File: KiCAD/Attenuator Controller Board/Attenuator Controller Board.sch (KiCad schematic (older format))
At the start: 21 parts, among them J1 Barrel_Jack_Switch, J10 Conn_01x24_Female, J2 Conn_01x02_Female, J9 Conn_01x24_Female, U12 Teensy3.6

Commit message: Rebuild schematic- git can be frustrating sometimes
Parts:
- removed H10: MountingHole_Pad, Custom Footprints:Ref_only, symbol Mechanical:MountingHole_Pad
- removed H9: MountingHole_Pad, Custom Footprints:M2_standoff_ground_via, symbol Mechanical:MountingHole_Pad
- removed J1: Barrel_Jack_Switch, Custom Footprints:DC-jack_54-00165, symbol Connector:Barrel_Jack_Switch
- removed J2: Conn_01x02_Female, Custom Footprints:Wire_Pad, symbol Connector:Conn_01x02_Female
- added C1, C2: 10µF, Custom Footprints:0508_Capacitor, symbol Device:C_Small
- added J5: DSub9, Custom Footprints:K202XHT-E9P-N, symbol Attenuator-Controller-Board-rescue:K202XHT-E9P-N-Custom_parts
- added R1: R_Small, Resistor_SMD:R_0603_1608Metric, symbol Device:R_Small
- J1: renamed from J9; symbol Custom_parts:Conn_01x24_Female -> Attenuator-Controller-Board-rescue:Conn_01x24_Female-Custom_parts
- J2: renamed from J?; value DSub_15_HD_-_200-015-263R001 -> DSub_15_HD; footprint Custom:DSub_15_HD-200-015-263R001 -> Custom Footprints:200-015-263R001; symbol Custom_parts:DSub_15_HD_-_200-015-263R001 -> Attenuator-Controller-Board-rescue:DSub_15_HD_-_200-015-263R001-Custom_parts
- J3, J4: renamed from J?; value K202XHT-E9P-N -> DSub9; footprint Custom:K202XHT-E9P-N -> Custom Footprints:K202XHT-E9P-N; symbol Custom_parts:K202XHT-E9P-N -> Attenuator-Controller-Board-rescue:K202XHT-E9P-N-Custom_parts
- J6: renamed from J10; symbol Custom_parts:Conn_01x24_Female -> Attenuator-Controller-Board-rescue:Conn_01x24_Female-Custom_parts
- U1: renamed from U?; footprint SOIC_7T8TA_DIO -> Custom Footprints:ZXMHC3A01T8TA; symbol Custom_parts:ZXMHC3A01T8TA -> Attenuator-Controller-Board-rescue:ZXMHC3A01T8TA-Custom_parts; Manufacturer (none) -> Diodes Incorporated; Part # (none) -> ZXMHC3A01T8TA
- U2: renamed from U?; footprint Custom:ADM3307EARUZ -> Custom Footprints:ADM3307EARUZ; symbol Custom_parts:ADM3307EARU-REEL7 -> Attenuator-Controller-Board-rescue:ADM3307EARU-REEL7-Custom_parts
- U3: renamed from U12; symbol Custom_parts:Teensy3.6 -> Attenuator-Controller-Board-rescue:Teensy3.6-Custom_parts
- gave numbers to parts that had none: 6
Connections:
- net labels added: Enable, Motor1, Motor2, RS-232_RXD3, RS-232_TXD3, Serial3-RX, Serial3-TX, Shutdown
- net labels removed: Ident(+)
- wire segments 75 -> 74
- no-connect marks 61 -> 63

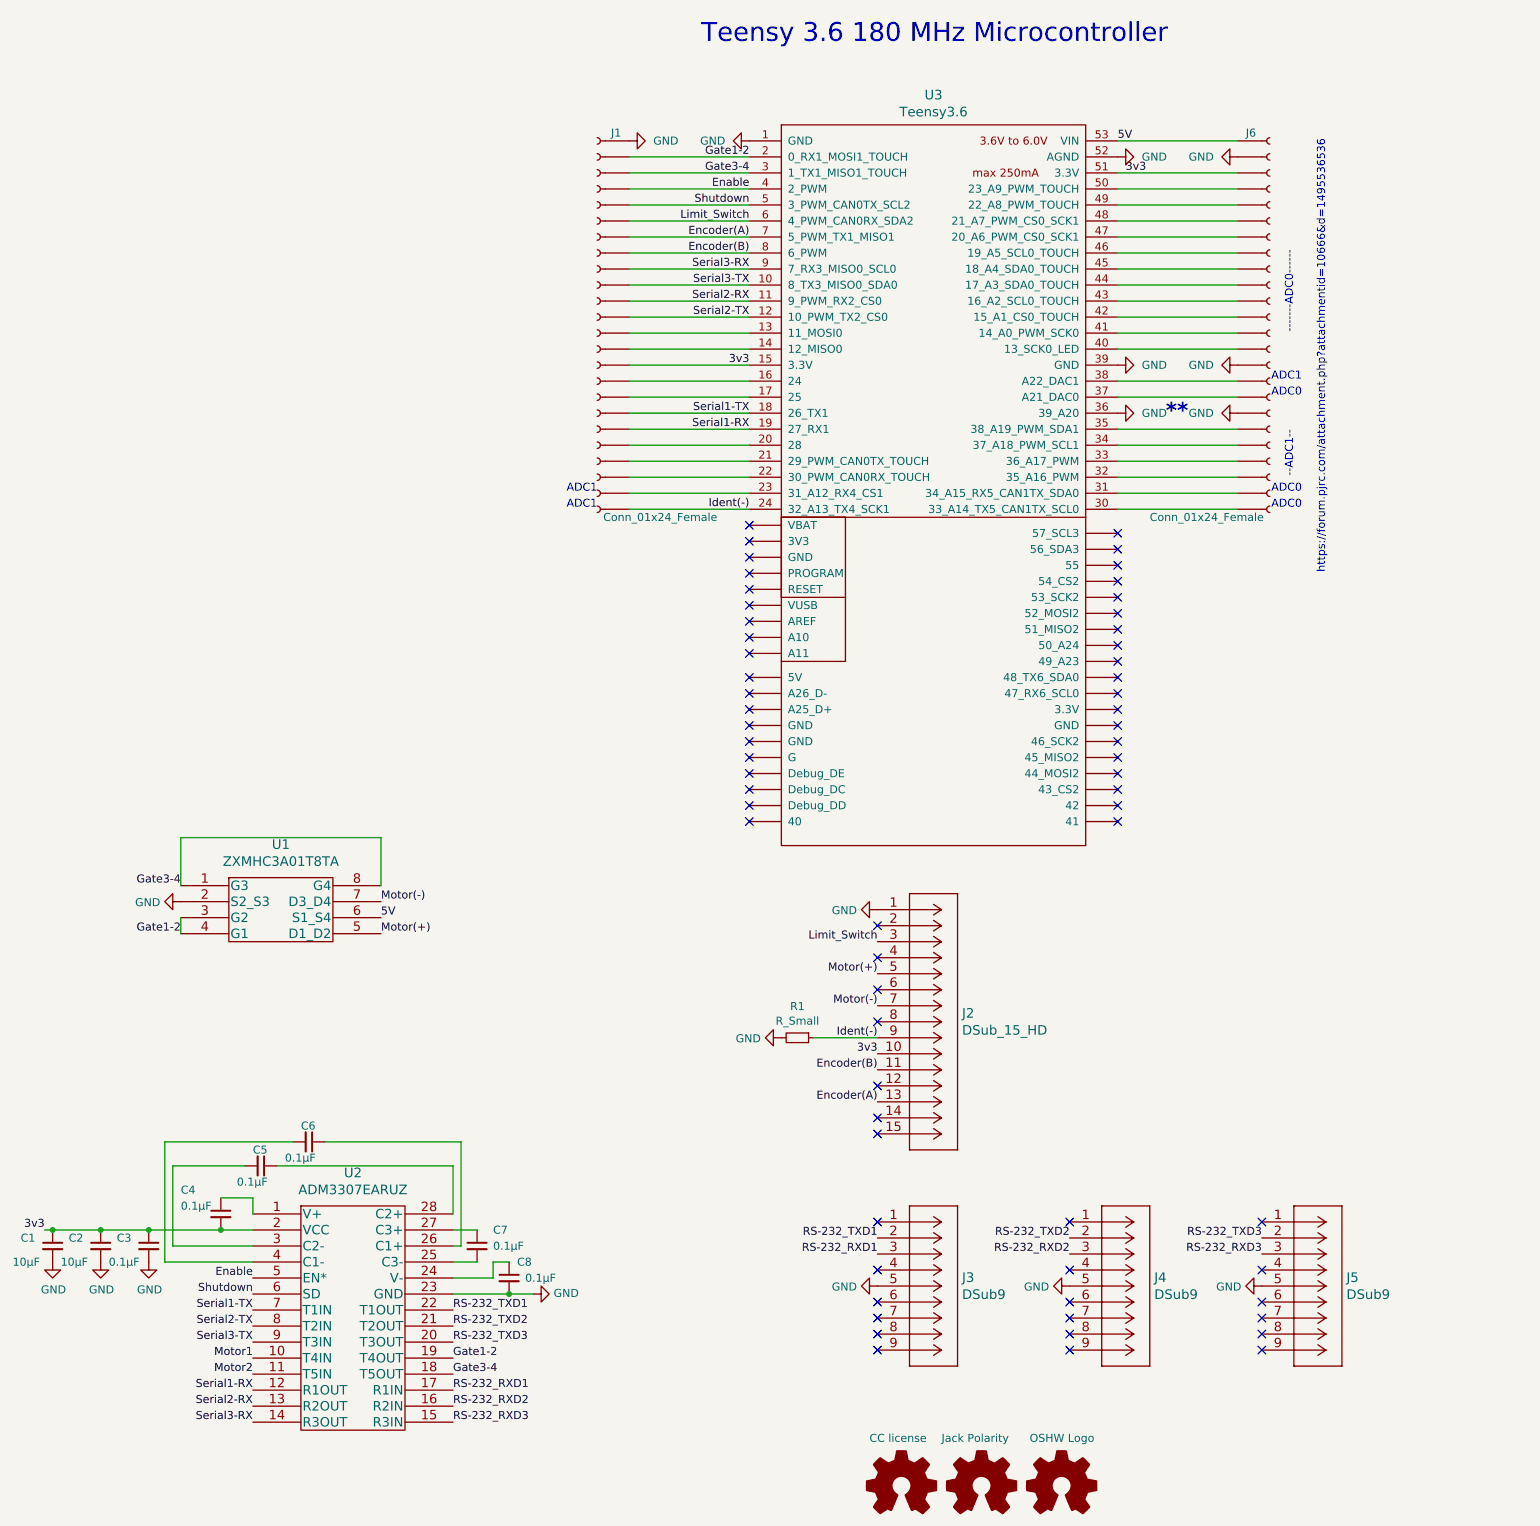
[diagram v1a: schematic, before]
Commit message: BNC clamps and alarm added
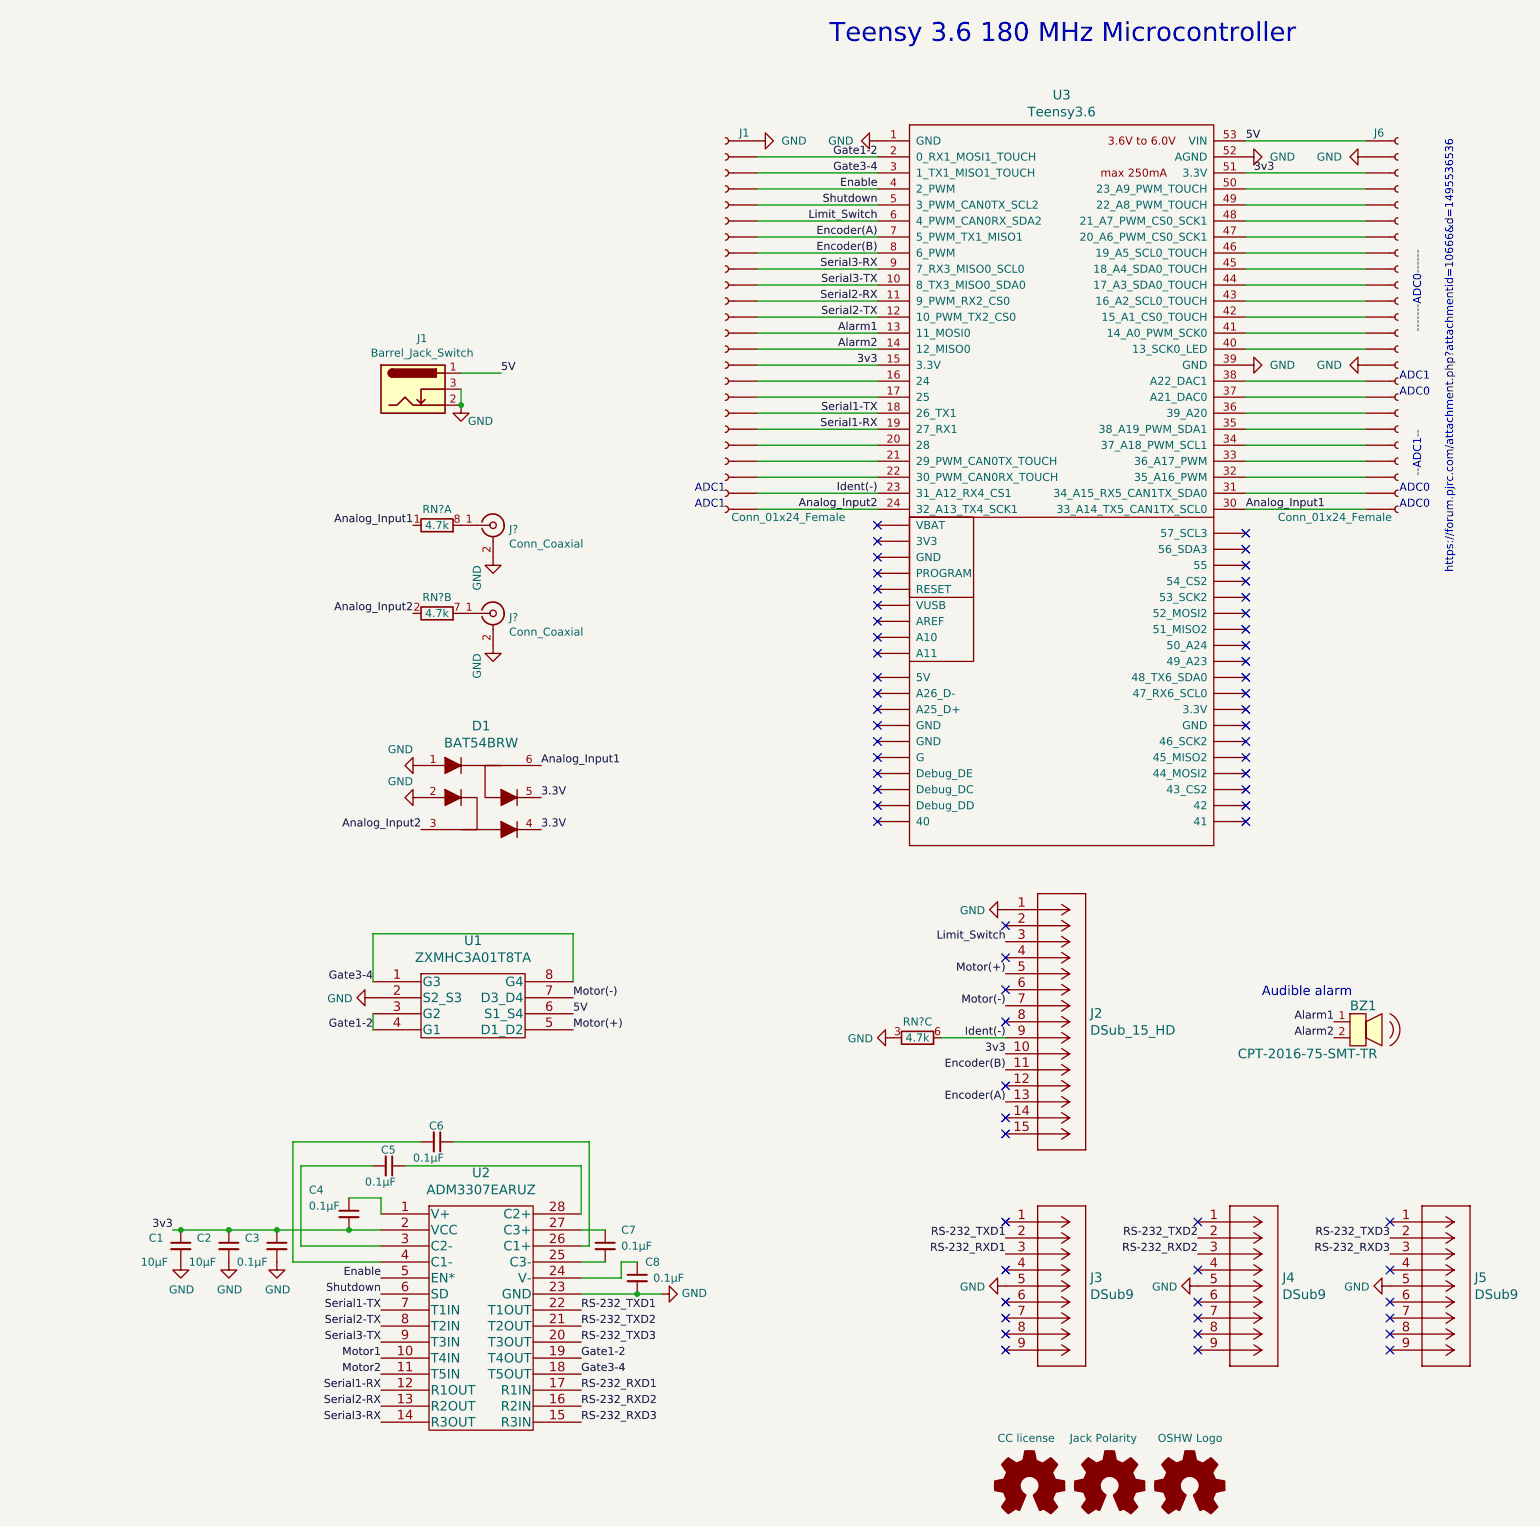
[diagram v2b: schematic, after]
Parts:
- removed R1: R_Small, Resistor_SMD:R_0603_1608Metric, symbol Device:R_Small
- added BZ1: CPT-2016-75-SMT-TR, Custom Footprints:SMT-0940-T-3V-R_9x9_alarm, symbol Custom_parts:CPT-2016-75-SMT-TR
- added D1: BAT54BRW, Package_TO_SOT_SMD:SOT-363_SC-70-6, symbol Custom_parts:BAT54BRW
- added J1: Barrel_Jack_Switch, Custom Footprints:DC-jack_54-00165, symbol Connector:Barrel_Jack_Switch
- added J? (x2): Conn_Coaxial, Custom Footprints:112640, symbol Connector:Conn_Coaxial
- added RN? (x3): 4.7k, Resistor_SMD:R_Array_Convex_4x1206, symbol Device:R_Pack04_Split
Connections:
- net 5V: now also J1.1
- net GND: now also D1.1, D1.2, J1.2, J1.3, J?.2 (Ext), J?.2 (Ext), RN?.3 (R3.1); no longer U3.36 (39_A20)
- net Ident(-): now also U3.23 (31_A12_RX4_CS1), RN?.6 (R3.2); no longer U3.24 (32_A13_TX4_SCK1)
- net Alarm1: now reaches J1.~, U3.13 (11_MOSI0)
- net Alarm1: now also BZ1.1
- net Alarm2: now reaches J1.~, U3.14 (12_MISO0)
- net Alarm2: now also BZ1.2
- net Analog_Input1: now reaches J6.~, U3.30 (33_A14_TX5_CAN1TX_SCL0)
- net Analog_Input1: now also D1.6, RN?.1 (R1.1)
- new net: J?.1 (In), RN?.8 (R1.2)
- new net: J6.~, U3.36 (39_A20)
- new net: J?.1 (In), RN?.7 (R2.2)
- new net 3.3V: D1.4, D1.5
- new net Analog_Input2: D1.3, J1.~, RN?.2 (R2.1), U3.24 (32_A13_TX4_SCK1)
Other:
- note added: "Audible alarm"
- note removed: "**"
- moved on the sheet: C1, C2, C3, C4, C5, C6, C7, C8, J2, J3, J4, J5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

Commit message: Initial PCB layout
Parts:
- added H1, H2, H3, H4: MountingHole, Custom Footprints:1_4-20_Clearance_hole, symbol Mechanical:MountingHole
- gave numbers to parts that had none: 3
- renumbered J1 to J4, J2 to J5, J3 to J6, J4 to J7, J5 to J8, J6 to J9, U2 to U1, U1 to U2
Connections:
- net NC24: now reaches J4.~, U3.16 (24)
- net NC25: now reaches J4.~, U3.17 (25)
- net NC28: now reaches J4.~, U3.20 (28)
- net NC29: now reaches J4.~, U3.21 (29_PWM_CAN0TX_TOUCH)
- net NC30: now reaches J4.~, U3.22 (30_PWM_CAN0RX_TOUCH)
- net NC34: now reaches J9.~, U3.31 (34_A15_RX5_CAN1TX_SDA0)
- net NC35: now reaches J9.~, U3.32 (35_A16_PWM)
- net NC36: now reaches J9.~, U3.33 (36_A17_PWM)
- net NC37: now reaches J9.~, U3.34 (37_A18_PWM_SCL1)
- net NC38: now reaches J9.~, U3.35 (38_A19_PWM_SDA1)
- net NC39: now reaches J9.~, U3.36 (39_A20)
- net NC_DAC0: now reaches J9.~, U3.37 (A21_DAC0)
- net NC_DAC1: now reaches J9.~, U3.38 (A22_DAC1)
- net NC13: now reaches J9.~, U3.40 (13_SCK0_LED)
- net NC14: now reaches J9.~, U3.41 (14_A0_PWM_SCK0)
- net NC15: now reaches J9.~, U3.42 (15_A1_CS0_TOUCH)
- net NC16: now reaches J9.~, U3.43 (16_A2_SCL0_TOUCH)
- net NC17: now reaches J9.~, U3.44 (17_A3_SDA0_TOUCH)
- net NC18: now reaches J9.~, U3.45 (18_A4_SDA0_TOUCH)
- net NC19: now reaches J9.~, U3.46 (19_A5_SCL0_TOUCH)
- net NC20: now reaches J9.~, U3.47 (20_A6_PWM_CS0_SCK1)
- net NC21: now reaches J9.~, U3.48 (21_A7_PWM_CS0_SCK1)
- net NC22: now reaches J9.~, U3.49 (22_A8_PWM_TOUCH)
- net NC23: now reaches J9.~, U3.50 (23_A9_PWM_TOUCH)
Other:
- moved on the sheet: BZ1, C1, C2, C3, C4, C5, C6, C7, C8, D1, J1, J2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

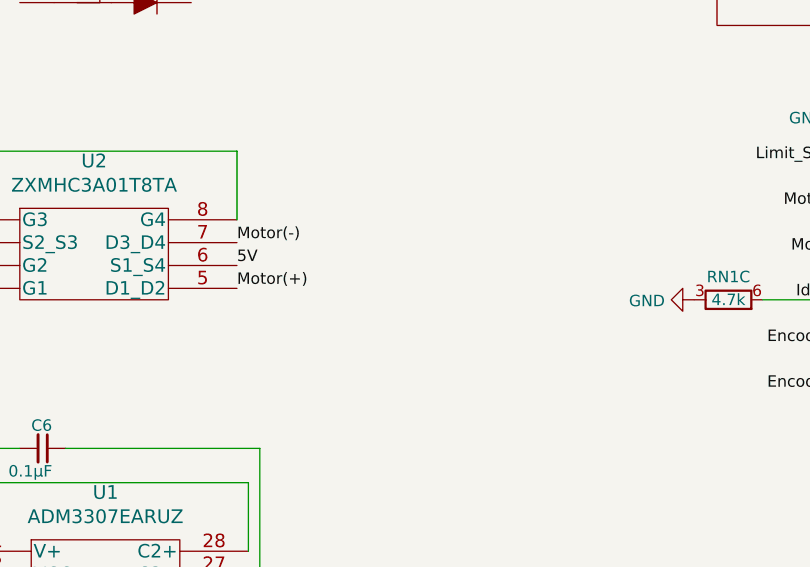
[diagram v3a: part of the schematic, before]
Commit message: Schottky diode protecting Vin->motor added
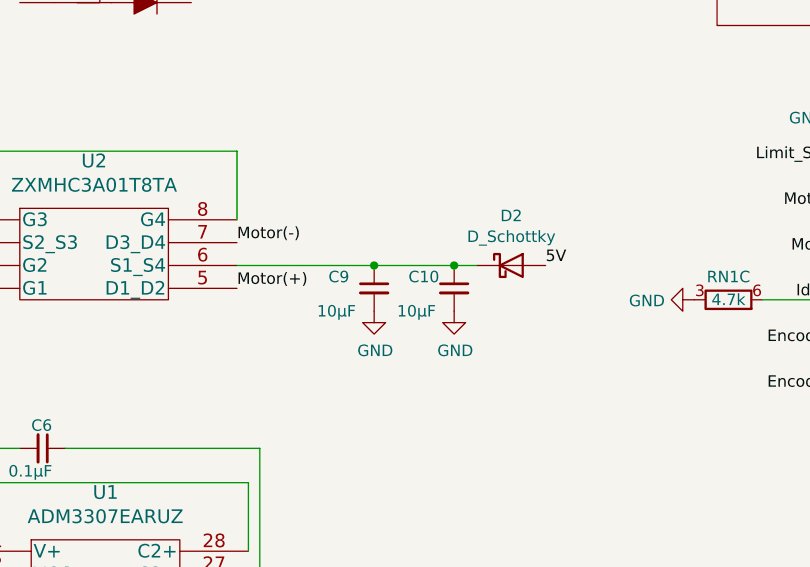
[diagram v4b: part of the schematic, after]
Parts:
- added C10, C9: 10µF, Custom Footprints:0508_Capacitor, symbol Device:C_Small
- added D2: D_Schottky, Custom Footprints:DO-214BA, symbol Device:D_Schottky
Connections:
- net 5V: now also D2.2 (A); no longer U2.6 (S1_S4)
- net GND: now also C10.2, C9.2
- new net: C10.1, C9.1, D2.1 (K), U2.6 (S1_S4)
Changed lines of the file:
@@
 Text Label 9600 6650 0    50   ~ 0
 Motor(-)
-Text Label 9600 6750 0    50   ~ 0
+Text Label 10950 6750 0    50   ~ 0
 5V
 Text Label 11500 1400 2    50   ~ 0
@@
 Text Label 13800 3500 0    50   ~ 0
 NC34
+$Comp
+L Device:C_Small C10
+U 1 1 620BEBA5
+P 10550 6850
+F 0 "C10" H 10350 6900 50  0000 L CNN
+F 1 "10µF" H 10300 6750 50  0000 L CNN
+F 2 "Custom Footprints:0508_Capacitor" H 10550 6850 50  0001 C CNN
+F 3 "https://www.digikey.com/en/products/detail/taiyo-yuden/LWK212BJ106MD-T/2763363" H 10550 6850 50  0001 C CNN
+F 4 "Taiyo Yuden" H 10550 6850 50  0001 C CNN "Manufacturer"
+F 5 "LWK212BJ106MD-T" H 10550 6850 50  0001 C CNN "Part #"
+	1    10550 6850
+	1    0    0    -1
+$EndComp
+$Comp
+L Device:C_Small C9
+U 1 1 620C1117
+P 10200 6850
+F 0 "C9" H 10000 6900 50  0000 L CNN
+F 1 "10µF" H 9950 6750 50  0000 L CNN
+F 2 "Custom Footprints:0508_Capacitor" H 10200 6850 50  0001 C CNN
+F 3 "https://www.digikey.com/en/products/detail/taiyo-yuden/LWK212BJ106MD-T/2763363" H 10200 6850 50  0001 C CNN
+F 4 "Taiyo Yuden" H 10200 6850 50  0001 C CNN "Manufacturer"
+F 5 "LWK212BJ106MD-T" H 10200 6850 50  0001 C CNN "Part #"
+	1    10200 6850
+	1    0    0    -1
+$EndComp
+Wire Wire Line
+	9600 6750 10200 6750
+$Comp
+L power:GND #PWR0101
+U 1 1 620C5042
+P 10200 6950
+F 0 "#PWR0101" H 10200 6700 50  0001 C CNN
+F 1 "GND" H 10205 6777 50  0000 C CNN
+F 2 "" H 10200 6950 50  0001 C CNN
+F 3 "" H 10200 6950 50  0001 C CNN
+	1    10200 6950
+	1    0    0    -1
+$EndComp
+$Comp
+L power:GND #PWR0102
+U 1 1 620C5B03
+P 10550 6950
+F 0 "#PWR0102" H 10550 6700 50  0001 C CNN
+F 1 "GND" H 10555 6777 50  0000 C CNN
+F 2 "" H 10550 6950 50  0001 C CNN
+F 3 "" H 10550 6950 50  0001 C CNN
+	1    10550 6950
+	1    0    0    -1
+$EndComp
+Connection ~ 10200 6750
+Connection ~ 10550 6750
+Wire Wire Line
+	10550 6750 10650 6750
+Wire Wire Line
+	10200 6750 10550 6750
+$Comp
+L Device:D_Schottky D2
+U 1 1 620CBB13
+P 10800 6750
+F 0 "D2" H 10800 6967 50  0000 C CNN
+F 1 "D_Schottky" H 10800 6876 50  0000 C CNN
+F 2 "Custom Footprints:DO-214BA" H 10800 6750 50  0001 C CNN
+F 3 "https://media.digikey.com/pdf/Data%20Sheets/Microsemi%20PDFs/LSM115J.pdf" H 10800 6750 50  0001 C CNN
+F 4 "Microchip Technology" H 10800 6750 50  0001 C CNN "Manufacturer"
+F 5 "LSM115JE3/TR13" H 10800 6750 50  0001 C CNN "Part #"
+	1    10800 6750
+	1    0    0    -1
+$EndComp
 $EndSCHEMATC

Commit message: Started on traces
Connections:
- net RS-232_RXD1: now also U1.15 (R3IN); no longer U1.17 (R1IN)
- net RS-232_RXD3: now also U1.17 (R1IN); no longer U1.15 (R3IN)
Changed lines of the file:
@@
 Text Label 9650 8600 0    50   ~ 0
 RS-232_TXD1
-Text Label 9650 9100 0    50   ~ 0
+Text Label 9650 9300 0    50   ~ 0
 RS-232_RXD1
 Text Label 13850 1500 0    50   ~ 0
@@
 Text Label 8400 9000 2    50   ~ 0
 Motor2
-Text Label 9650 9300 0    50   ~ 0
+Text Label 9650 9100 0    50   ~ 0
 RS-232_RXD3
 Text Label 8400 9300 2    50   ~ 0
